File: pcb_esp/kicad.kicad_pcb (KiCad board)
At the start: 2 copper layers, 25 parts, among them J1 Prog Pads, J2 SLP, J3 SHT21, J4 BH1750, M1 TP4056Module, SW1 RST, SW2 PRG, U1 LT1963, U2 ESP-12F

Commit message: WIP first board for ESP and regulator
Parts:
- removed BT1: 18650, Battery:BatteryHolder_MPD_BH-18650-PC2
- removed M1: TP4056Module, footprints:TP4056_Module
- added J5: PWRIN, Connector_Wire:SolderWirePad_1x01_Drill1mm, F.Cu at (50.0, 58.0)
- added J6: GND, Connector_Wire:SolderWirePad_1x01_Drill1mm, F.Cu at (90.0, 58.0)
- moved J4 105.5 mm to (24.4, 24.4)
- moved J2 94.6 mm to (109.0, 25.0), turned to 90 degrees
- moved J3 94.6 mm to (43.9, 24.9)
- moved C5 78.1 mm to (87.0, 38.0), turned to 270 degrees
- moved C4 73.7 mm to (93.0, 39.0), turned to 270 degrees
- moved R10 68.5 mm to (72.0, 32.0), turned to 0 degrees
- moved SW1 68.5 mm to (72.0, 26.0), turned to 180 degrees
- moved SW2 68.1 mm to (80.0, 26.0), turned to 180 degrees
- moved R9 68.0 mm to (80.0, 32.0), turned to 0 degrees
- moved J1 67.8 mm to (115.0, 52.0), turned to 270 degrees
- moved U2 65.2 mm to (108.0, 39.1), turned to 270 degrees
- moved C3 59.2 mm to (37.0, 41.0), turned to 0 degrees
- moved R1 55.7 mm to (28.0, 55.0), turned to 270 degrees
- moved R8 51.0 mm to (99.0, 52.0), turned to 180 degrees
- moved R2 50.5 mm to (33.0, 56.0), turned to 0 degrees
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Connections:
- J2 pad 1: GND -> Net-(J2-Pad1)
- U2 pad 4: GND -> Net-(J2-Pad1)
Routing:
- net PWR: track 0.00 -> 50.7 mm
- net RST: track 0.00 -> 30.0 mm
- net Net-(C2-Pad1): track 0.00 -> 26.1 mm
- net Net-(R1-Pad2): track 0.00 -> 13.3 mm, vias 0 -> 2
- net GND: track 0.00 -> 10.9 mm
- net Net-(J2-Pad1): track 0.00 -> 7.93 mm
- net DTR: track 0.00 -> 6.93 mm
- net Net-(R9-Pad1): track 0.00 -> 6.29 mm
- net Net-(R10-Pad1): track 0.00 -> 6.29 mm
- net TXD: track 0.00 -> 5.72 mm
- net Net-(R8-Pad1): track 0.00 -> 5.69 mm
- net RXD: track 0.00 -> 5.49 mm
- net Net-(C1-Pad2): track 0.00 -> 4.49 mm
- net SDA: track 0.00 -> 3.03 mm, vias 0 -> 1
- net SCL: vias 0 -> 1
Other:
- board outline added: 100 x 40 mm

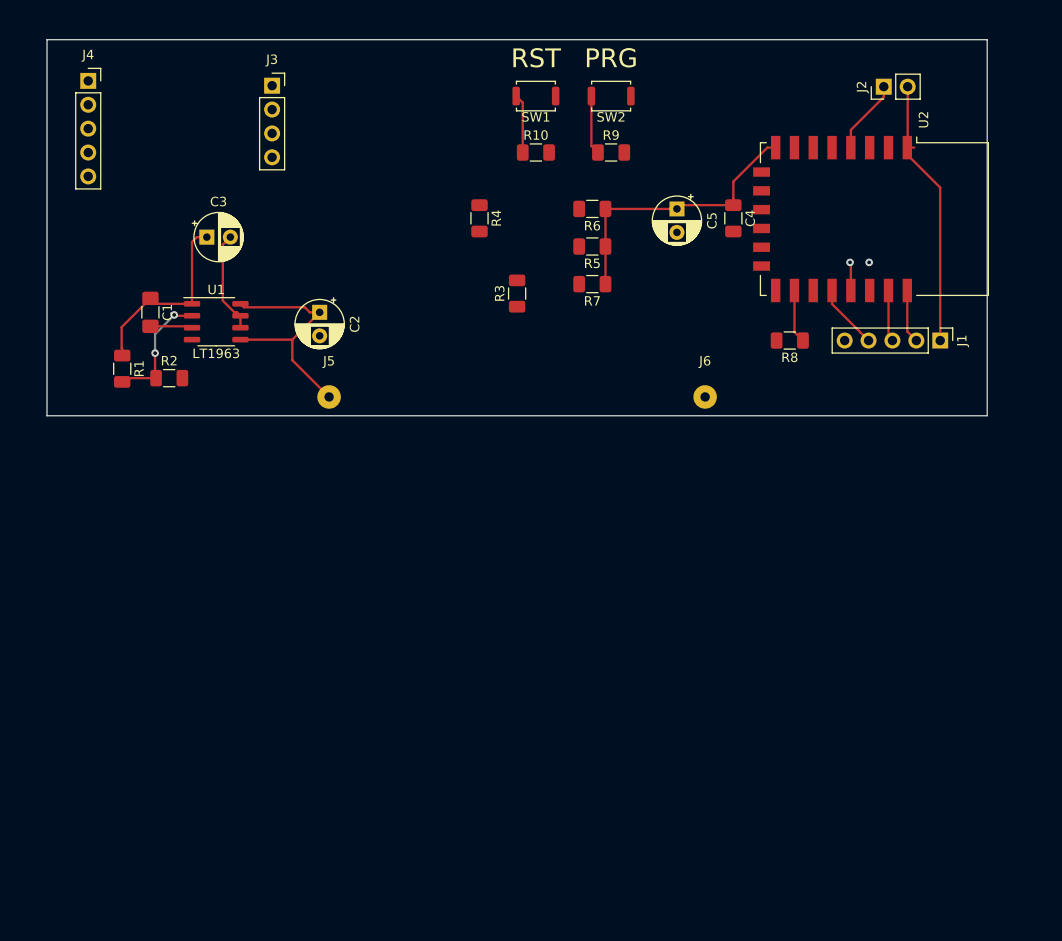
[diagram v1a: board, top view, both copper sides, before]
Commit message: Edge layer for to pcb, making it smaller (30 wide)
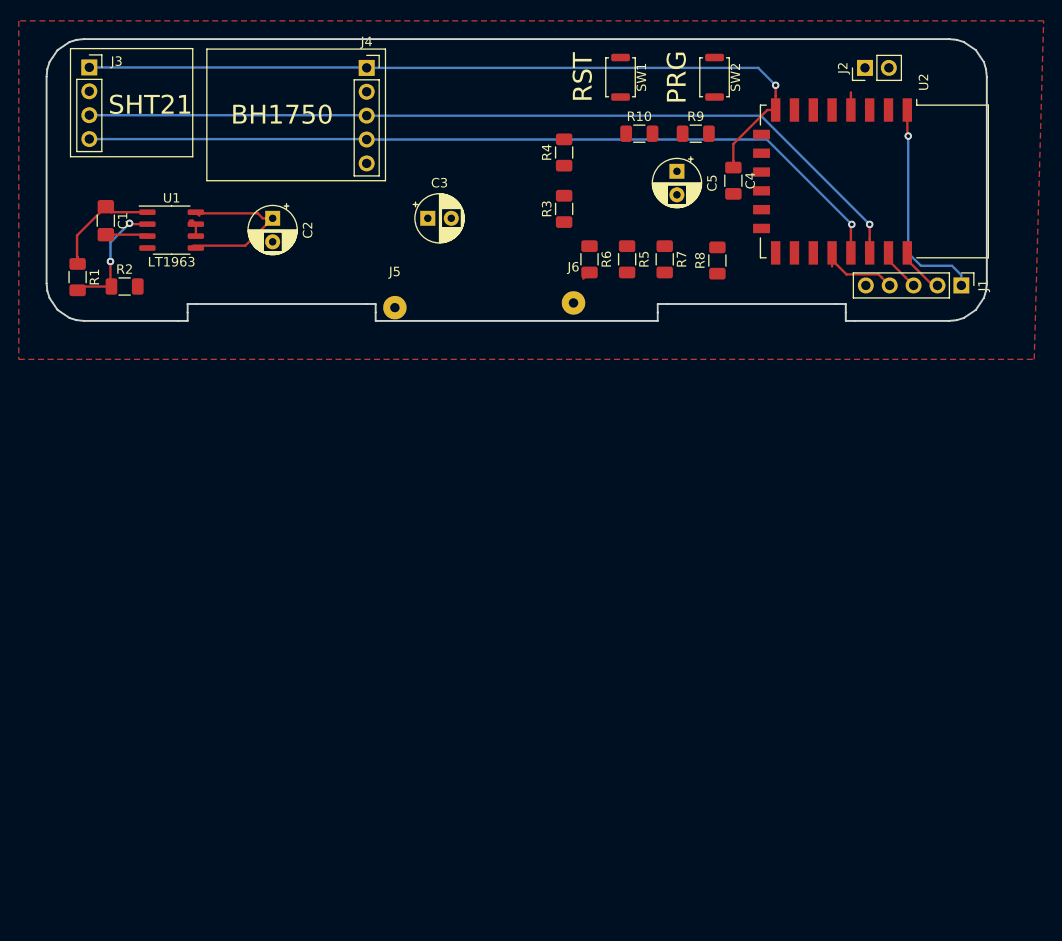
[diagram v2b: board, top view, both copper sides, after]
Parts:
- moved J4 29.6 mm to (54.0, 23.0)
- moved C3 23.6 mm to (60.5, 39.0)
- moved J3 19.5 mm to (24.5, 22.9)
- moved J6 17.2 mm to (76.0, 48.0)
- moved J5 11.8 mm to (57.0, 48.5)
- moved R8 11.5 mm to (91.3, 43.5), turned to 90 degrees
- moved R4 11.4 mm to (75.0, 32.0), turned to 90 degrees
- moved C2 11.2 mm to (44.0, 39.0)
- moved R10 11.2 mm to (83.0, 30.0)
- moved SW2 11.2 mm to (91.0, 24.0), turned to 270 degrees
- moved U1 10.8 mm to (33.3, 40.3)
- moved C1 10.8 mm to (26.3, 39.3)
- moved R1 10.8 mm to (23.3, 45.3)
- moved R2 10.8 mm to (28.3, 46.3)
- moved R3 10.3 mm to (75.0, 38.0)
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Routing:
- net SCL: track 0.00 -> 90.8 mm
- net SDA: track 3.03 -> 87.9 mm
- net PWR: track 50.7 -> 97.5 mm, vias 0 -> 1
- net GND: track 10.9 -> 2.14 mm
- net Net-(C2-Pad1): track 26.1 -> 18.4 mm
- net Net-(R9-Pad1): track 6.29 -> 0.00 mm
- net Net-(R10-Pad1): track 6.29 -> 0.00 mm
- net Net-(J2-Pad1): track 7.93 -> 1.88 mm
- net Net-(R8-Pad1): track 5.69 -> 0.00 mm
- net RST: track 30.0 -> 25.5 mm, vias 0 -> 1
- net DTR: track 6.93 -> 9.44 mm
- net RXD: track 5.49 -> 4.57 mm
- net TXD: track 5.72 -> 5.08 mm
- added copper zone on F.Cu, net GND
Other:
- board size 100 x 40 mm -> 100 x 30 mm

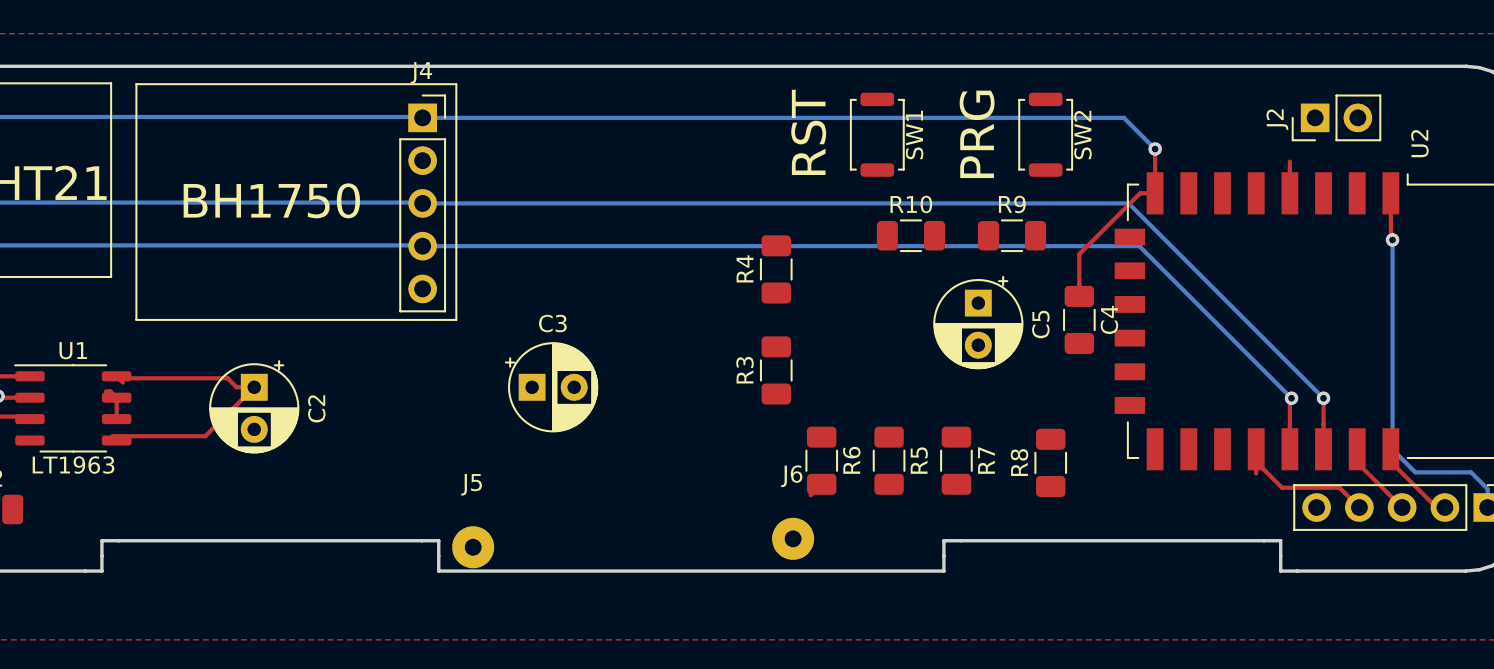
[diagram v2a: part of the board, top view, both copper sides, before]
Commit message: Add pads for power contacts and main mechanical connection
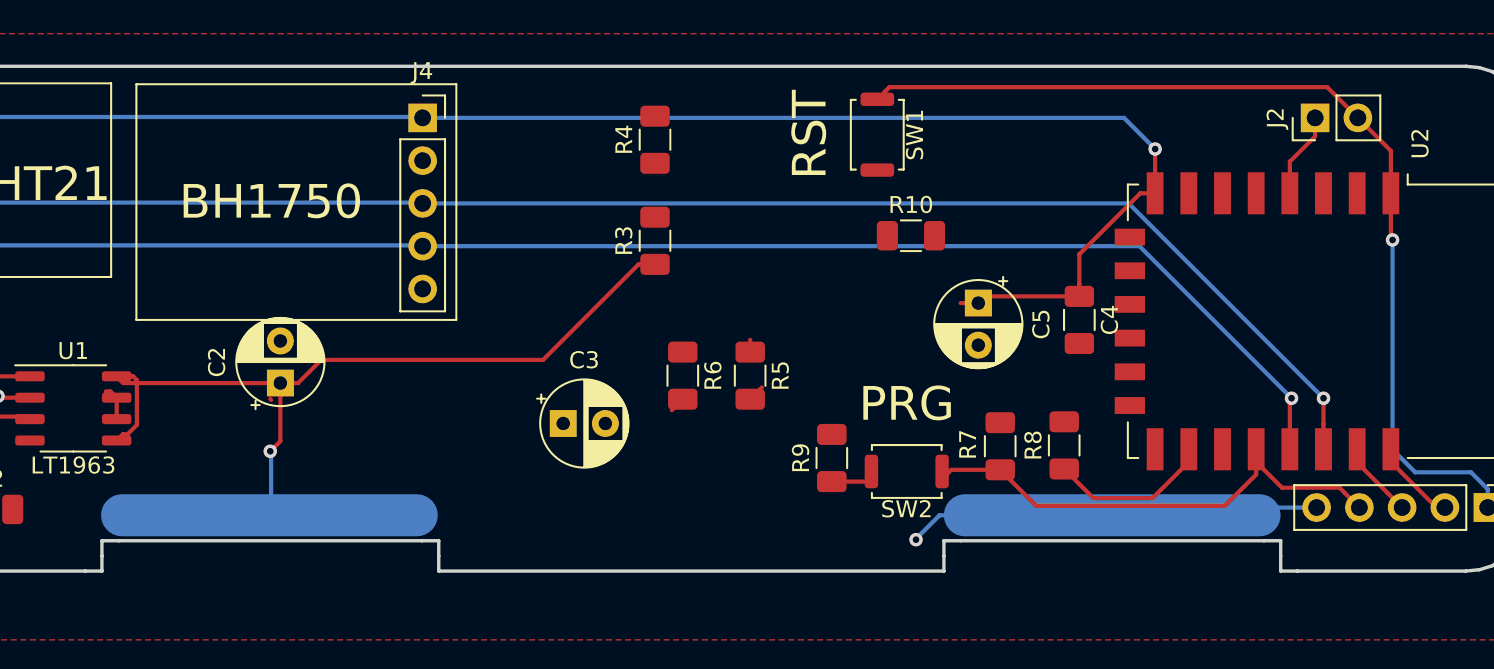
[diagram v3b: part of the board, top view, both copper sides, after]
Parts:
- J5: value PWRIN -> +; moved to B.Cu
- J6: moved to B.Cu
- moved SW2 21.6 mm to (82.8, 44.0), turned to 180 degrees
- moved J6 19.0 mm to (95.0, 46.6)
- moved R9 17.0 mm to (78.3, 43.2), turned to 90 degrees
- moved J5 12.2 mm to (44.9, 46.6)
- moved R3 10.5 mm to (67.8, 30.3)
- moved R4 10.5 mm to (67.8, 24.3)
- moved R5 9.67 mm to (73.5, 38.3)
- moved R6 9.67 mm to (69.5, 38.3)
- moved C3 2.84 mm to (62.4, 41.1)
- moved R7 2.74 mm to (88.3, 42.5)
- moved C2 1.57 mm to (45.5, 38.8), turned to 90 degrees
- moved R8 1.31 mm to (92.1, 42.5)
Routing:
- net RST: track 25.5 -> 60.4 mm
- net Net-(C2-Pad1): track 18.4 -> 49.0 mm, vias 0 -> 1
- net GND: track 2.14 -> 26.8 mm, vias 0 -> 1
- net DTR: track 9.44 -> 30.0 mm
- net Net-(R8-Pad1): track 0.00 -> 9.76 mm
- net PWR: track 97.5 -> 104.9 mm
- net Net-(J2-Pad1): track 1.88 -> 5.10 mm
- net Net-(R9-Pad1): track 0.00 -> 2.41 mm
- net Net-(R5-Pad2): track 0.00 -> 1.73 mm

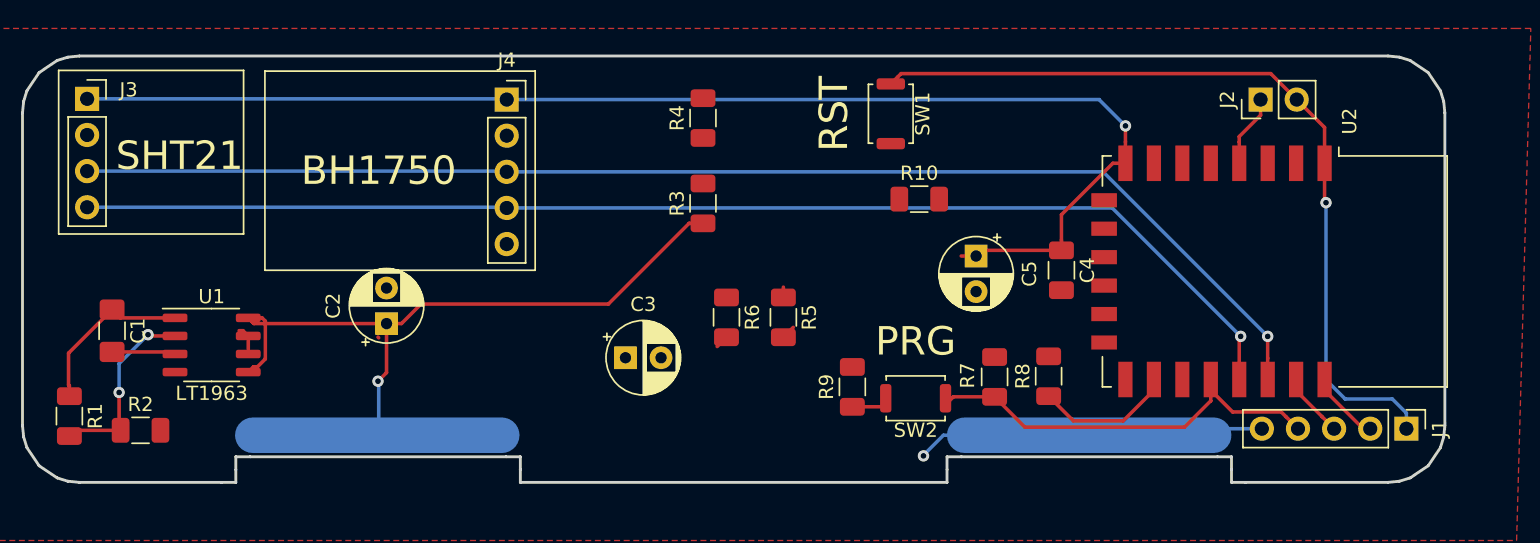
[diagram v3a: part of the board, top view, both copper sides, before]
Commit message: ESP module - placed and connected
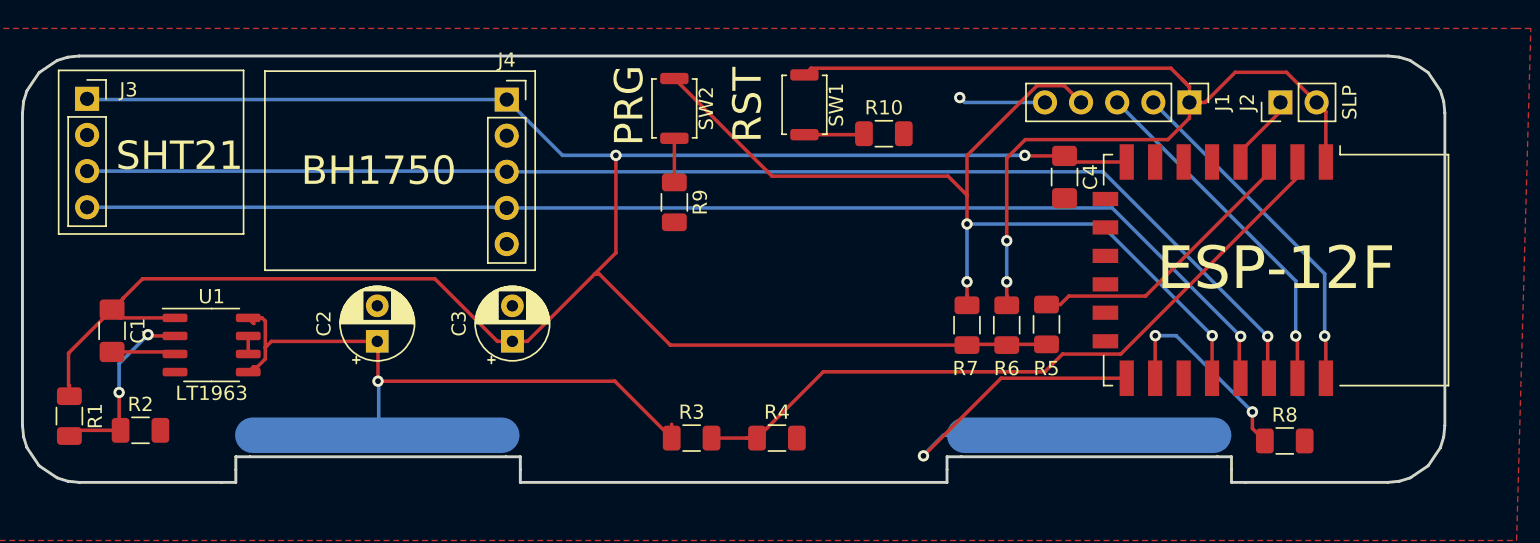
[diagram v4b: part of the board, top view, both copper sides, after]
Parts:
- removed C5: 470u, Capacitor_THT:CP_Radial_D5.0mm_P2.50mm
- C4: footprint Capacitor_SMD:C_1206_3216Metric -> Capacitor_SMD:C_1206_3216Metric_Pad1.42x1.75mm_HandSolder
- J5: value + -> PWRIN
- moved J1 27.5 mm to (102.0, 23.2)
- moved SW2 26.5 mm to (65.8, 23.6), turned to 270 degrees
- moved R4 23.1 mm to (73.0, 46.8), turned to 0 degrees
- moved R6 19.7 mm to (89.2, 38.9), turned to 90 degrees
- moved R5 18.5 mm to (91.9, 38.8), turned to 90 degrees
- moved R9 18.0 mm to (65.8, 30.2), turned to 270 degrees
- moved R8 17.2 mm to (108.7, 47.0), turned to 0 degrees
- moved R3 16.5 mm to (67.0, 46.8), turned to 0 degrees
- moved C3 8.03 mm to (54.4, 40.0), turned to 90 degrees
- moved C4 6.56 mm to (93.2, 28.4)
- moved SW1 6.10 mm to (74.9, 23.4)
- moved R10 5.23 mm to (80.5, 25.4)
- moved R7 4.12 mm to (86.4, 38.9), turned to 90 degrees
- moved J2 1.41 mm to (108.4, 23.2)
- moved C2 1.41 mm to (44.9, 40.0)
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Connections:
- net Net-(C1-Pad2) renamed /BYP
- net Net-(C2-Pad1) renamed /PWR+
- net Net-(J2-Pad1) renamed /GPIO16
- net Net-(R1-Pad2) renamed /ADJ
- net Net-(R5-Pad2) renamed /EN
- net Net-(R8-Pad1) renamed /GPIO15
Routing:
- net PWR: track 104.9 -> 168.4 mm, vias 1 -> 2
- net ADC: track 0.00 -> 49.9 mm
- net DTR: track 30.0 -> 70.0 mm, vias 0 -> 3
- net RXD: track 4.57 -> 25.4 mm, vias 0 -> 1
- net TXD: track 5.08 -> 25.2 mm, vias 0 -> 1
- net /EN: track 1.73 -> 21.3 mm
- net RST: track 60.4 -> 71.0 mm, vias 1 -> 2
- net GND: track 26.8 -> 37.0 mm, vias 1 -> 2
- net /GPIO15: track 9.76 -> 15.2 mm, vias 0 -> 2
- net /PWR+: track 49.0 -> 44.3 mm
- net Net-(R10-Pad1): track 0.00 -> 4.22 mm
- net Net-(R9-Pad1): track 2.41 -> 3.10 mm

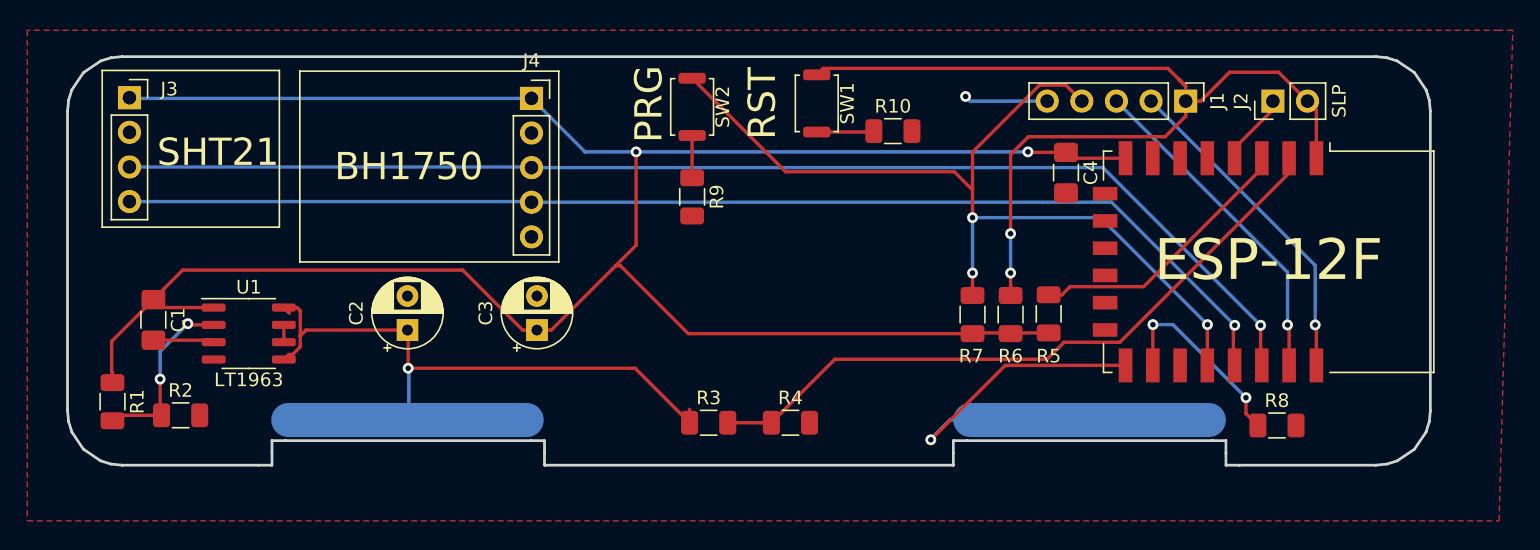
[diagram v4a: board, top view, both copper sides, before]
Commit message: Change button footprint, ad kicad logo.
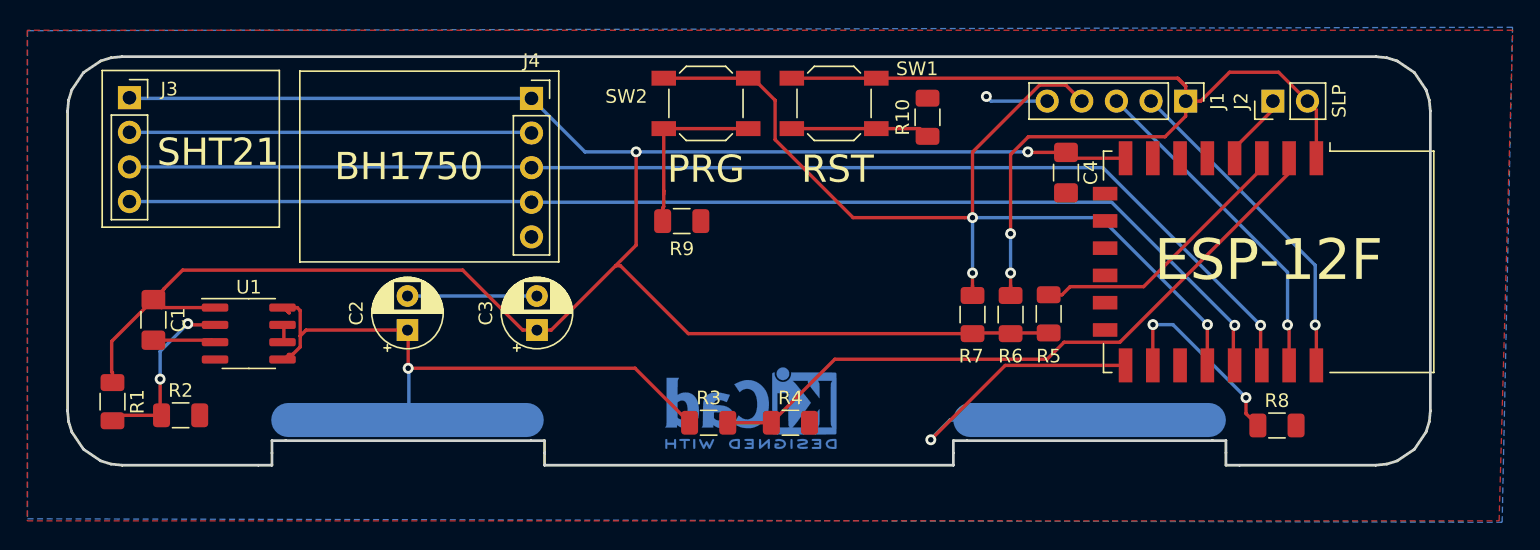
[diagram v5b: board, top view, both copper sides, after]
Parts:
- added REF**: KiCad-Logo2_5mm_Copper_Mask, logos:KiCad-Logo2_5mm_Copper_Mask, B.Cu at (70.1, 45.7)
- SW1, SW2: footprint Button_Switch_SMD:SW_Push_SPST_NO_Alps_SKRK -> Button_Switch_SMD:SW_SPST_SKQG_WithStem
- U1: footprint Package_SO:SO-8_3.9x4.9mm_P1.27mm -> Package_SO:SOIC-8_3.9x4.9mm_P1.27mm
- moved R10 2.74 mm to (83.1, 24.4), turned to 90 degrees
- moved R9 1.93 mm to (65.0, 32.0), turned to 0 degrees
- moved SW1 1.27 mm to (76.2, 23.4), turned to 0 degrees
- moved SW2 1.05 mm to (66.8, 23.4), turned to 0 degrees
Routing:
- net GND: track 37.0 -> 74.4 mm
- net Net-(R9-Pad1): track 3.10 -> 13.3 mm
- net Net-(R10-Pad1): track 4.22 -> 10.3 mm
- net DTR: track 70.0 -> 74.6 mm
- net RST: track 71.0 -> 72.3 mm
- net /PWR+: track 44.3 -> 43.3 mm
- added copper zone on B.Cu, net GND

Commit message: Small, mostly visual, improvements
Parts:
- added Ref**: Val**, logos:roommonitor-rev, F.Cu at (67.6, 38.6)
- J1: value Prog Pads -> PRG
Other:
- board text added: "@josefadamcik"
- board text added: "http://josef-adamcik.cz"
